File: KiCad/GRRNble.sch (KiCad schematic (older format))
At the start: 48 parts, among them J1 JST_SH_06, Q1 DMG3415U, Q2 BSS138, Q3 DMG3415U, SW1 SW_Push, SW2 SW_Push, SW3 SW_Push, U1 R5F100LJAFB, U2 BUZZER, U3 SSD1306, U4 MCP73831, U5 RN4020, U6 NJM2865F33, Y1 32.768k

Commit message: change PCB status
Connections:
- net STAT: now also U1.21 (P31/TI03/TO03/INTP4/(PCLBUZ0)); no longer U1.29 (P70/KR0/SCK21/SCL21)
- net SW1: now also U1.41 (P15/SCK20/SCL20/(TI02)/(TO02)); no longer U1.43 (P13/TxD2/SO20/(SDAA0)/(TI04)/(TO04))
- net SW2: now also U1.43 (P13/TxD2/SO20/(SDAA0)/(TI04)/(TO04)); no longer U1.41 (P15/SCK20/SCL20/(TI02)/(TO02))
- net VDD: now also U1.29 (P70/KR0/SCK21/SCL21); no longer U1.21 (P31/TI03/TO03/INTP4/(PCLBUZ0))
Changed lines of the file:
@@
 Text GLabel 14300 5700 0    60   Input ~ 0
 SW3
+Text GLabel 7900 5300 2    60   Input ~ 0
+SW1
 Text GLabel 7900 5100 2    60   Input ~ 0
-SW1
-Text GLabel 7900 5300 2    60   Input ~ 0
 SW2
 Text GLabel 7900 5400 2    60   Input ~ 0
@@
 Wire Wire Line
 	8050 650  8050 750
-Text GLabel 3450 5800 0    60   Input ~ 0
+Text GLabel 3400 5000 0    60   Input ~ 0
 STAT
 Wire Wire Line
@@
 Text GLabel 3250 1150 0    60   Input ~ 0
 STAT
-Text GLabel 3400 5000 0    60   Input ~ 0
+Text GLabel 3450 5800 0    60   Input ~ 0
 VDD
 Wire Wire Line

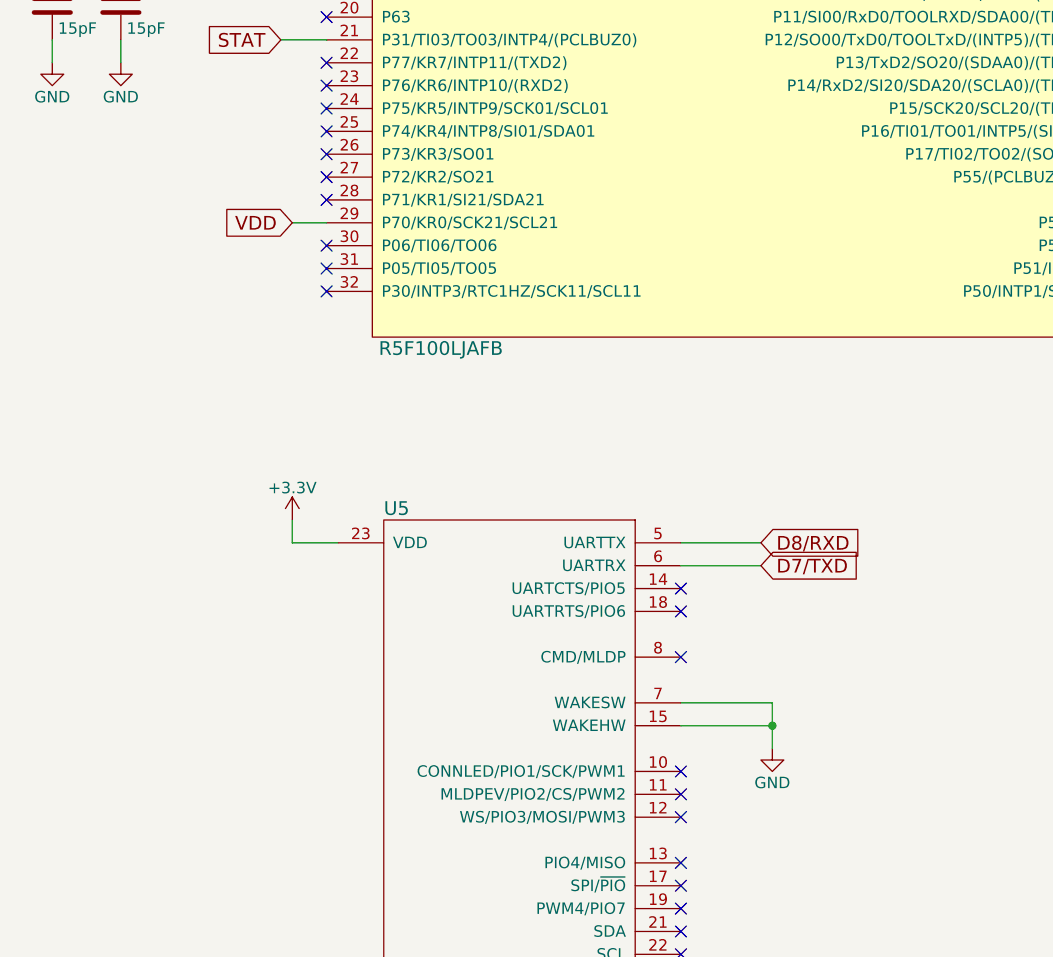
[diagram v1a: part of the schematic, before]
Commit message: change schematic layout
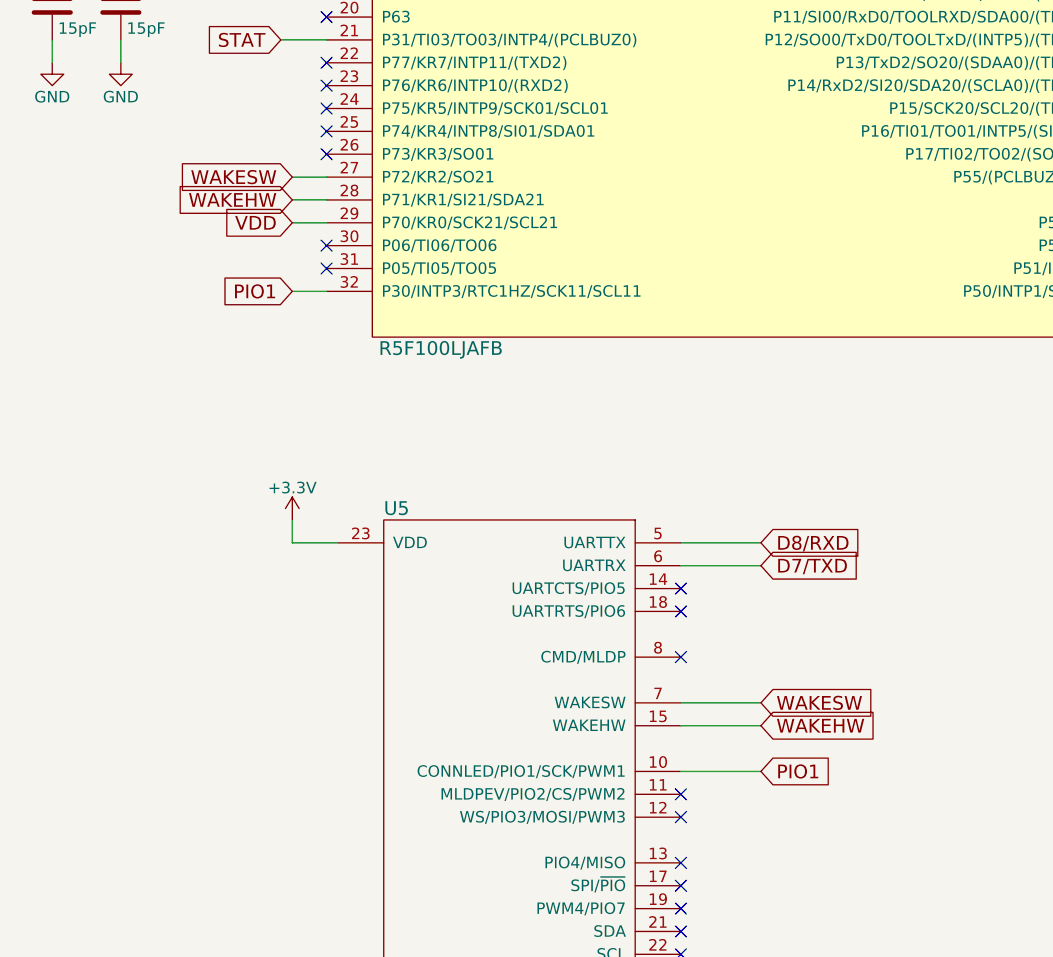
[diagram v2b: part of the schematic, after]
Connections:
- net GND: no longer U5.15 (WAKEHW), U5.7 (WAKESW)
- net WAKESW: now reaches U1.27 (P72/KR2/SO21)
- net WAKESW: now also U5.7 (WAKESW)
- net WAKEHW: now reaches U1.28 (P71/KR1/SI21/SDA21)
- net WAKEHW: now also U5.15 (WAKEHW)
- net PIO1: now reaches U1.32 (P30/INTP3/RTC1HZ/SCK11/SCL11)
- net PIO1: now also U5.10 (CONNLED/PIO1/SCK/PWM1)
- no-connect marks 52 -> 48
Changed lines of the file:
@@
 NoConn ~ 3600 5400
 NoConn ~ 3600 5500
-NoConn ~ 3600 5600
-NoConn ~ 3600 5700
-NoConn ~ 3600 6100
 NoConn ~ 3600 5900
 NoConn ~ 3600 6000
@@
 NoConn ~ 5150 7500
 NoConn ~ 5150 7700
-$Comp
-L power:GND #PWR019
-U 1 1 5B1FF555
-P 5550 8100
-F 0 "#PWR019" H 5550 7850 50  0001 C CNN
-F 1 "GND" H 5550 7950 50  0000 C CNN
-F 2 "" H 5550 8100 50  0001 C CNN
-F 3 "" H 5550 8100 50  0001 C CNN
-	1    5550 8100
-	1    0    0    -1
-$EndComp
-NoConn ~ 5150 8200
 NoConn ~ 5150 8300
 NoConn ~ 5150 8400
@@
 	5500 7300 5150 7300
 Wire Wire Line
-	5150 8000 5550 8000
-Wire Wire Line
-	5550 7900 5550 8000
-Wire Wire Line
-	5150 7900 5550 7900
-Connection ~ 5550 8000
-Wire Wire Line
 	3650 9600 3450 9600
 Wire Wire Line
@@
 	13950 1100 13950 900
 Wire Wire Line
-	5550 8000 5550 8100
-Wire Wire Line
 	3450 9600 3450 9700
 Wire Wire Line
@@
 Wire Wire Line
 	3450 5800 3600 5800
+Text GLabel 3450 5600 0    60   Input ~ 0
+WAKESW
+Text GLabel 3450 5700 0    60   Input ~ 0
+WAKEHW
+Wire Wire Line
+	3450 5600 3600 5600
+Wire Wire Line
+	3600 5700 3450 5700
+Text GLabel 5500 7900 2    60   Input ~ 0
+WAKESW
+Text GLabel 5500 8000 2    60   Input ~ 0
+WAKEHW
+Wire Wire Line
+	5150 7900 5500 7900
+Wire Wire Line
+	5500 8000 5150 8000
+Text GLabel 3450 6100 0    60   Input ~ 0
+PIO1
+Wire Wire Line
+	3450 6100 3600 6100
+Text GLabel 5500 8200 2    60   Input ~ 0
+PIO1
+Wire Wire Line
+	5150 8200 5500 8200
 $EndSCHEMATC

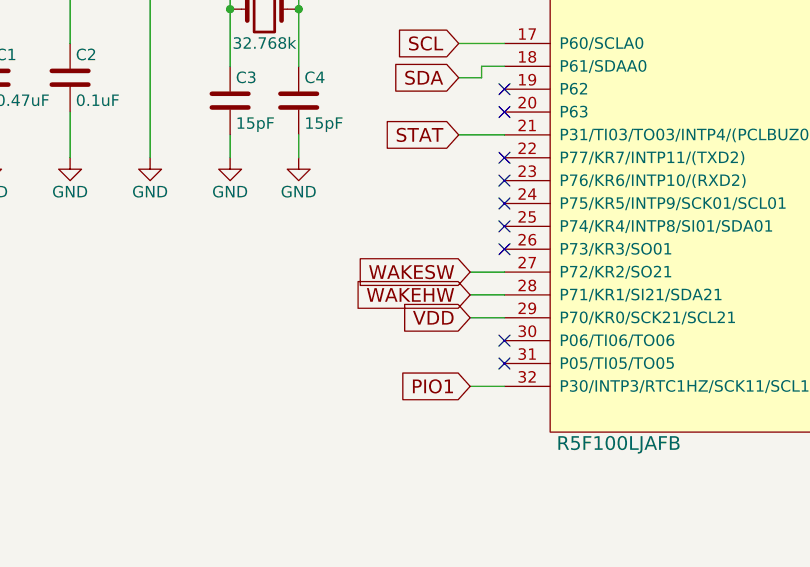
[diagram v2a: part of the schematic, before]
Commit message: change PCB layout
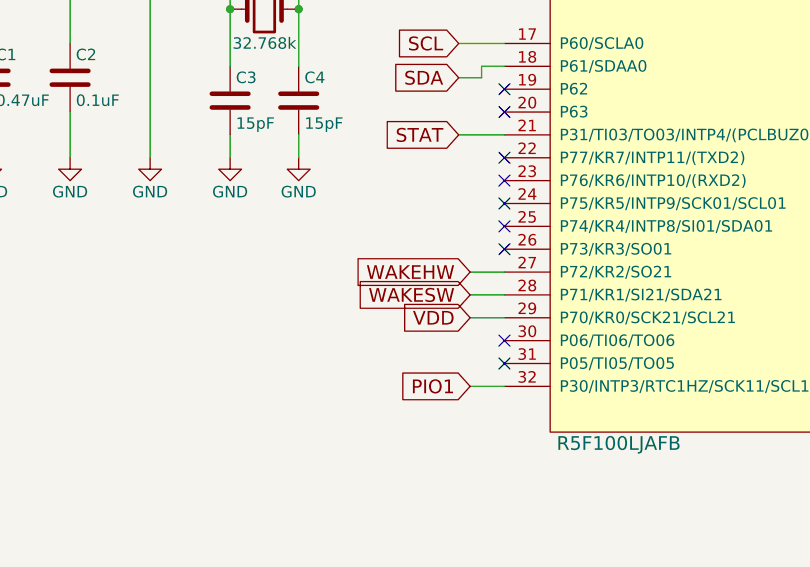
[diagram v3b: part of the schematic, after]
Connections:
- net WAKEHW: now also U1.27 (P72/KR2/SO21); no longer U1.28 (P71/KR1/SI21/SDA21)
- net WAKESW: now also U1.28 (P71/KR1/SI21/SDA21); no longer U1.27 (P72/KR2/SO21)
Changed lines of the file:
@@
 Wire Wire Line
 	3450 5800 3600 5800
+Text GLabel 3450 5700 0    60   Input ~ 0
+WAKESW
 Text GLabel 3450 5600 0    60   Input ~ 0
-WAKESW
-Text GLabel 3450 5700 0    60   Input ~ 0
 WAKEHW
 Wire Wire Line

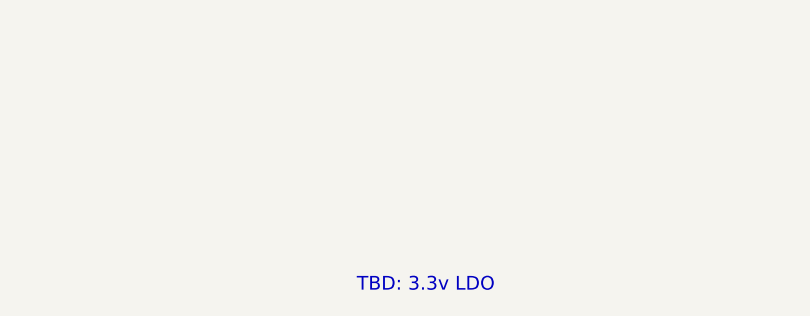
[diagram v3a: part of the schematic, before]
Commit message: add schematic
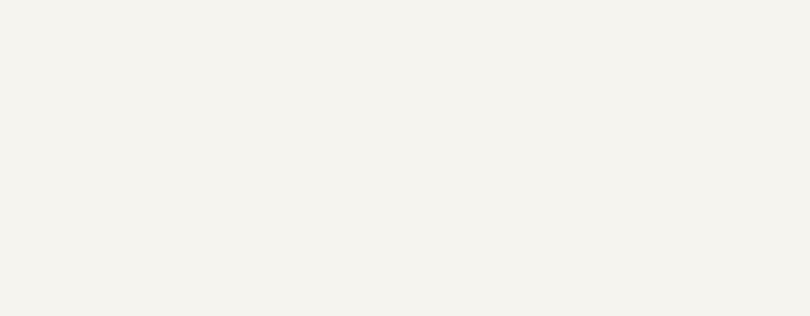
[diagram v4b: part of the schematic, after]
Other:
- note removed: "TBD: 3.3v LDO"
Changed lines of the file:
@@
 encoding utf-8
 Sheet 1 1
-Title ""
+Title "GRRNble"
 Date ""
 Rev ""
@@
 $EndComp
 Text Notes 12550 10150 2    60   ~ 0
-TBD: 3.3v LDO
 $Comp
 L misc:NJM2865F33 U6

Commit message: WIP:Change schematic
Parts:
- removed C14: 1.0uF, Capacitors_SMD:C_0805_HandSoldering, symbol GRRNble-rescue:C
- removed R11: 100k, Resistors_SMD:R_0805_HandSoldering, symbol GRRNble-rescue:R
- removed U6: NJM2865F33, TO_SOT_Packages_SMD:SOT-23-5_HandSoldering, symbol misc:NJM2865F33
- added R11: 100k, Resistor_SMD:R_0805_2012Metric_Pad1.15x1.40mm_HandSolder, symbol Device:R
- added U6: MCP1703A-3302_SOT23, Package_TO_SOT_SMD:SOT-23, symbol Regulator_Linear:MCP1703A-3302_SOT23
- C15: value 0.1uF -> 1.0uF
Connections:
- net +3V3: now also U6.2 (VO)
- net +5V: now also U6.3 (VI)
- net GND: now also R11.2, U6.1 (GND)
- net SW2: now also U1.42 (P14/RxD2/SI20/SDA20/(SCLA0)/(TI03)/(TO03)); no longer U1.43 (P13/TxD2/SO20/(SDAA0)/(TI04)/(TO04))
- net at U2.1 (+): now also U1.43 (P13/TxD2/SO20/(SDAA0)/(TI04)/(TO04)); no longer U1.42 (P14/RxD2/SI20/SDA20/(SCLA0)/(TI03)/(TO03))
- net at C12.1, D1.2 (A), J1.4 (P4)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: now also R11.1
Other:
- moved on the sheet: C16, U2
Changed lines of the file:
@@
 Text GLabel 7900 5300 2    60   Input ~ 0
 SW1
-Text GLabel 7900 5100 2    60   Input ~ 0
+Text GLabel 7900 5200 2    60   Input ~ 0
 SW2
 Text GLabel 7900 5400 2    60   Input ~ 0
@@
 L power:GND #PWR015
 U 1 1 5AE9D4C6
-P 9450 5500
-F 0 "#PWR015" H 9450 5250 50  0001 C CNN
-F 1 "GND" H 9450 5350 50  0000 C CNN
-F 2 "" H 9450 5500 50  0001 C CNN
-F 3 "" H 9450 5500 50  0001 C CNN
-	1    9450 5500
+P 9450 5400
+F 0 "#PWR015" H 9450 5150 50  0001 C CNN
+F 1 "GND" H 9450 5250 50  0000 C CNN
+F 2 "" H 9450 5400 50  0001 C CNN
+F 3 "" H 9450 5400 50  0001 C CNN
+	1    9450 5400
 	1    0    0    -1
 $EndComp
@@
 L misc:BUZZER U2
 U 1 1 5AE9F4E8
-P 8900 5300
-F 0 "U2" H 8900 5400 60  0000 C CNN
-F 1 "BUZZER" H 8900 5300 60  0000 C CNN
-F 2 "misc:BZ7025_3pin" H 8900 5300 60  0001 C CNN
-F 3 "" H 8900 5300 60  0000 C CNN
-	1    8900 5300
+P 8900 5200
+F 0 "U2" H 8900 5300 60  0000 C CNN
+F 1 "BUZZER" H 8900 5200 60  0000 C CNN
+F 2 "misc:BZ7025_3pin" H 8900 5200 60  0001 C CNN
+F 3 "" H 8900 5200 60  0000 C CNN
+	1    8900 5200
 	1    0    0    -1
 $EndComp
@@
 $EndComp
 $Comp
-L GRRNble-rescue:C C14
-U 1 1 5B209940
-P 6700 1450
-F 0 "C14" H 6725 1550 50  0000 L CNN
-F 1 "1.0uF" H 6725 1350 50  0000 L CNN
-F 2 "Capacitors_SMD:C_0805_HandSoldering" H 6738 1300 50  0001 C CNN
-F 3 "" H 6700 1450 50  0001 C CNN
-	1    6700 1450
-	1    0    0    -1
-$EndComp
-$Comp
 L power:GND #PWR027
 U 1 1 5B209AFE
-P 6700 1700
-F 0 "#PWR027" H 6700 1450 50  0001 C CNN
-F 1 "GND" H 6700 1550 50  0000 C CNN
-F 2 "" H 6700 1700 50  0001 C CNN
-F 3 "" H 6700 1700 50  0001 C CNN
-	1    6700 1700
+P 5850 1700
+F 0 "#PWR027" H 5850 1450 50  0001 C CNN
+F 1 "GND" H 5850 1550 50  0000 C CNN
+F 2 "" H 5850 1700 50  0001 C CNN
+F 3 "" H 5850 1700 50  0001 C CNN
+	1    5850 1700
 	1    0    0    -1
 $EndComp
@@
 L power:+3.3V #PWR028
 U 1 1 5B209E7F
-P 11800 1050
-F 0 "#PWR028" H 11800 900 50  0001 C CNN
-F 1 "+3.3V" H 11800 1190 50  0000 C CNN
-F 2 "" H 11800 1050 50  0001 C CNN
-F 3 "" H 11800 1050 50  0001 C CNN
-	1    11800 1050
+P 11500 1050
+F 0 "#PWR028" H 11500 900 50  0001 C CNN
+F 1 "+3.3V" H 11500 1190 50  0000 C CNN
+F 2 "" H 11500 1050 50  0001 C CNN
+F 3 "" H 11500 1050 50  0001 C CNN
+	1    11500 1050
 	1    0    0    -1
 $EndComp
 Text Notes 12550 10150 2    60   ~ 0
-$Comp
-L misc:NJM2865F33 U6
-U 1 1 5B20FC5D
-P 10600 1350
-F 0 "U6" H 10600 1350 60  0000 C CNN
-F 1 "NJM2865F33" H 10600 1650 60  0000 C CNN
-F 2 "TO_SOT_Packages_SMD:SOT-23-5_HandSoldering" H 10600 1350 60  0001 C CNN
-F 3 "" H 10600 1350 60  0001 C CNN
-	1    10600 1350
-	1    0    0    -1
-$EndComp
 $Comp
 L GRRNble-rescue:C C15
@@
 P 9400 1350
 F 0 "C15" H 9425 1450 50  0000 L CNN
-F 1 "0.1uF" H 9425 1250 50  0000 L CNN
+F 1 "1.0uF" H 9425 1250 50  0000 L CNN
 F 2 "Capacitors_SMD:C_0805_HandSoldering" H 9438 1200 50  0001 C CNN
 F 3 "" H 9400 1350 50  0001 C CNN
@@
 Connection ~ 15050 5450
 Wire Wire Line
-	7400 5200 8500 5200
-Wire Wire Line
-	9300 5200 9450 5200
-Wire Wire Line
-	9450 5200 9450 5500
+	7400 5100 8500 5100
+Wire Wire Line
+	9300 5100 9450 5100
+Wire Wire Line
+	9450 5100 9450 5400
 Wire Wire Line
 	14650 900  14650 750
@@
 	8050 1050 8050 1700
 Wire Wire Line
-	6700 1700 6700 1600
-Wire Wire Line
 	6700 1050 6700 1200
 Connection ~ 6700 1200
 Wire Wire Line
-	11800 1200 11800 1050
+	11500 1200 11500 1050
 Wire Wire Line
 	7150 1200 7150 1050
@@
 Wire Wire Line
 	6000 950  6000 1200
-$Comp
-L GRRNble-rescue:R R11
-U 1 1 5B2116AD
-P 9800 1350
-F 0 "R11" V 9880 1350 50  0000 C CNN
-F 1 "100k" V 9800 1350 50  0000 C CNN
-F 2 "Resistors_SMD:R_0805_HandSoldering" V 9730 1350 50  0001 C CNN
-F 3 "" H 9800 1350 50  0001 C CNN
-	1    9800 1350
-	1    0    0    -1
-$EndComp
-Wire Wire Line
-	9800 1500 10000 1500
 Wire Wire Line
 	9050 1200 9400 1200
-Connection ~ 9800 1200
 Connection ~ 9400 1200
 $Comp
@@
 L power:GND #PWR030
 U 1 1 5B211EB3
-P 11200 1700
-F 0 "#PWR030" H 11200 1450 50  0001 C CNN
-F 1 "GND" H 11200 1550 50  0000 C CNN
-F 2 "" H 11200 1700 50  0001 C CNN
-F 3 "" H 11200 1700 50  0001 C CNN
-	1    11200 1700
-	1    0    0    -1
-$EndComp
-Wire Wire Line
-	11200 1500 11200 1700
+P 10300 1700
+F 0 "#PWR030" H 10300 1450 50  0001 C CNN
+F 1 "GND" H 10300 1550 50  0000 C CNN
+F 2 "" H 10300 1700 50  0001 C CNN
+F 3 "" H 10300 1700 50  0001 C CNN
+	1    10300 1700
+	1    0    0    -1
+$EndComp
+Wire Wire Line
+	10300 1500 10300 1700
 $Comp
 L GRRNble-rescue:C C16
 U 1 1 5B21210D
-P 11450 1350
-F 0 "C16" H 11475 1450 50  0000 L CNN
-F 1 "1.0uF" H 11475 1250 50  0000 L CNN
-F 2 "Capacitors_SMD:C_0805_HandSoldering" H 11488 1200 50  0001 C CNN
-F 3 "" H 11450 1350 50  0001 C CNN
-	1    11450 1350
+P 11150 1350
+F 0 "C16" H 11175 1450 50  0000 L CNN
+F 1 "1.0uF" H 11175 1250 50  0000 L CNN
+F 2 "Capacitors_SMD:C_0805_HandSoldering" H 11188 1200 50  0001 C CNN
+F 3 "" H 11150 1350 50  0001 C CNN
+	1    11150 1350
 	1    0    0    -1
 $EndComp
@@
 L power:GND #PWR031
 U 1 1 5B21224D
-P 11450 1700
-F 0 "#PWR031" H 11450 1450 50  0001 C CNN
-F 1 "GND" H 11450 1550 50  0000 C CNN
-F 2 "" H 11450 1700 50  0001 C CNN
-F 3 "" H 11450 1700 50  0001 C CNN
-	1    11450 1700
-	1    0    0    -1
-$EndComp
-Wire Wire Line
-	11450 1700 11450 1500
-Wire Wire Line
-	11200 1200 11450 1200
-Connection ~ 11450 1200
+P 11150 1700
+F 0 "#PWR031" H 11150 1450 50  0001 C CNN
+F 1 "GND" H 11150 1550 50  0000 C CNN
+F 2 "" H 11150 1700 50  0001 C CNN
+F 3 "" H 11150 1700 50  0001 C CNN
+	1    11150 1700
+	1    0    0    -1
+$EndComp
+Wire Wire Line
+	11150 1700 11150 1500
+Connection ~ 11150 1200
 $Comp
 L power:+5V #PWR032
@@
 $EndComp
 Wire Wire Line
-	3100 650  6200 650
-Wire Wire Line
 	7950 650  8050 650
 Wire Wire Line
@@
 	3250 1150 3500 1150
 Wire Wire Line
-	7400 5100 7900 5100
+	7400 5200 7900 5200
 Text GLabel 8350 650  2    60   Input ~ 0
 VDD
@@
 	6700 650  7650 650
 Wire Wire Line
-	6700 1200 6700 1300
-Wire Wire Line
 	6700 1200 7150 1200
 Wire Wire Line
 	7150 1200 7550 1200
 Wire Wire Line
-	9800 1200 10000 1200
-Wire Wire Line
-	9400 1200 9800 1200
-Wire Wire Line
-	11450 1200 11800 1200
+	11150 1200 11500 1200
 Wire Wire Line
 	10800 3300 10800 3250
@@
 Wire Wire Line
 	5150 8200 5500 8200
+$Comp
+L Regulator_Linear:MCP1703A-3302_SOT23 U6
+U 1 1 5C922623
+P 10300 1200
+F 0 "U6" H 10300 1442 50  0000 C CNN
+F 1 "MCP1703A-3302_SOT23" H 10300 1351 50  0000 C CNN
+F 2 "Package_TO_SOT_SMD:SOT-23" H 10300 1400 50  0001 C CNN
+F 3 "http://ww1.microchip.com/downloads/en/DeviceDoc/20005122B.pdf" H 10300 1150 50  0001 C CNN
+	1    10300 1200
+	1    0    0    -1
+$EndComp
+Wire Wire Line
+	9400 1200 10000 1200
+Wire Wire Line
+	10600 1200 11150 1200
+$Comp
+L Device:R R11
+U 1 1 5CA9E88E
+P 5850 1350
+F 0 "R11" H 5920 1396 50  0000 L CNN
+F 1 "100k" H 5920 1305 50  0000 L CNN
+F 2 "Resistor_SMD:R_0805_2012Metric_Pad1.15x1.40mm_HandSolder" V 5780 1350 50  0001 C CNN
+F 3 "~" H 5850 1350 50  0001 C CNN
+	1    5850 1350
+	1    0    0    -1
+$EndComp
+Wire Wire Line
+	5850 650  6200 650
+Wire Wire Line
+	3100 650  5850 650
+Connection ~ 5850 650
+Wire Wire Line
+	5850 1500 5850 1700
+Wire Wire Line
+	5850 1200 5850 650
 $EndSCHEMATC
